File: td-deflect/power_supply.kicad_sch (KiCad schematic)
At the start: 60 parts, among them J13 Conn_01x02_Male, J14 Conn_01x02_Male, J15 Conn_01x02_Male, J18 Conn_01x02_Male, J2 Conn_01x02_Male, J8 Conn_01x02_Male, J9 Conn_01x02_Male, Q12 C2M0045170D, Q13 BSZ42DN25NS3GATMA1, U13 MCP1416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

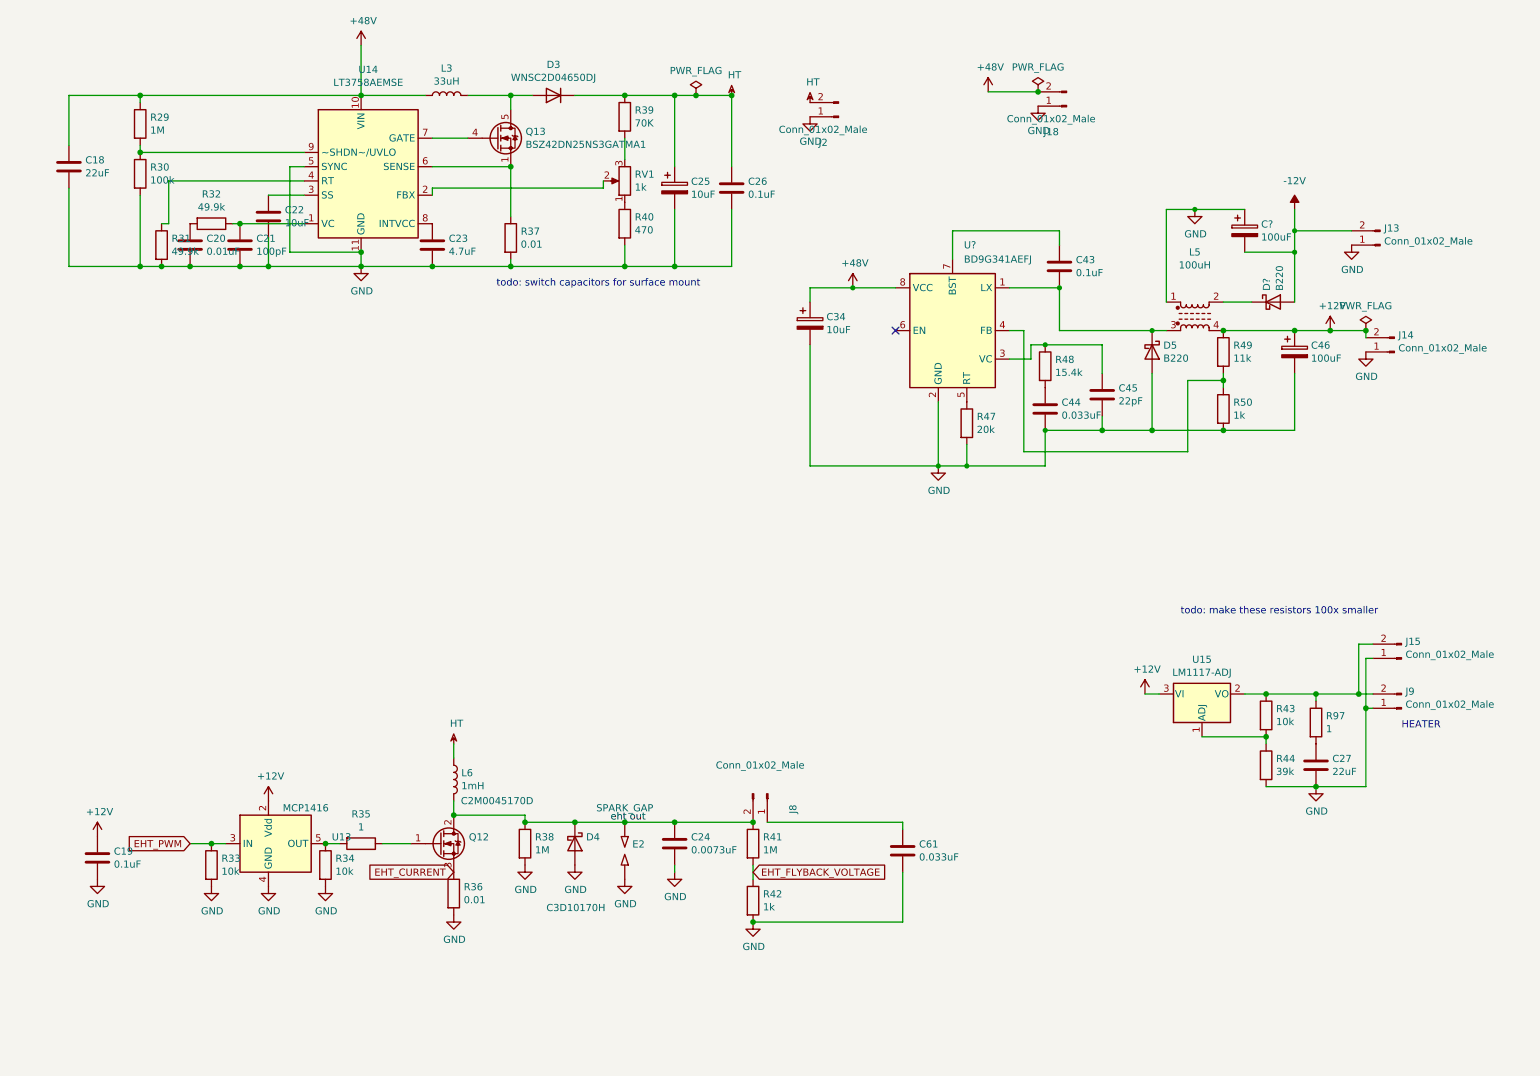
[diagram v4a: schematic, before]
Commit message: add switching heater supply
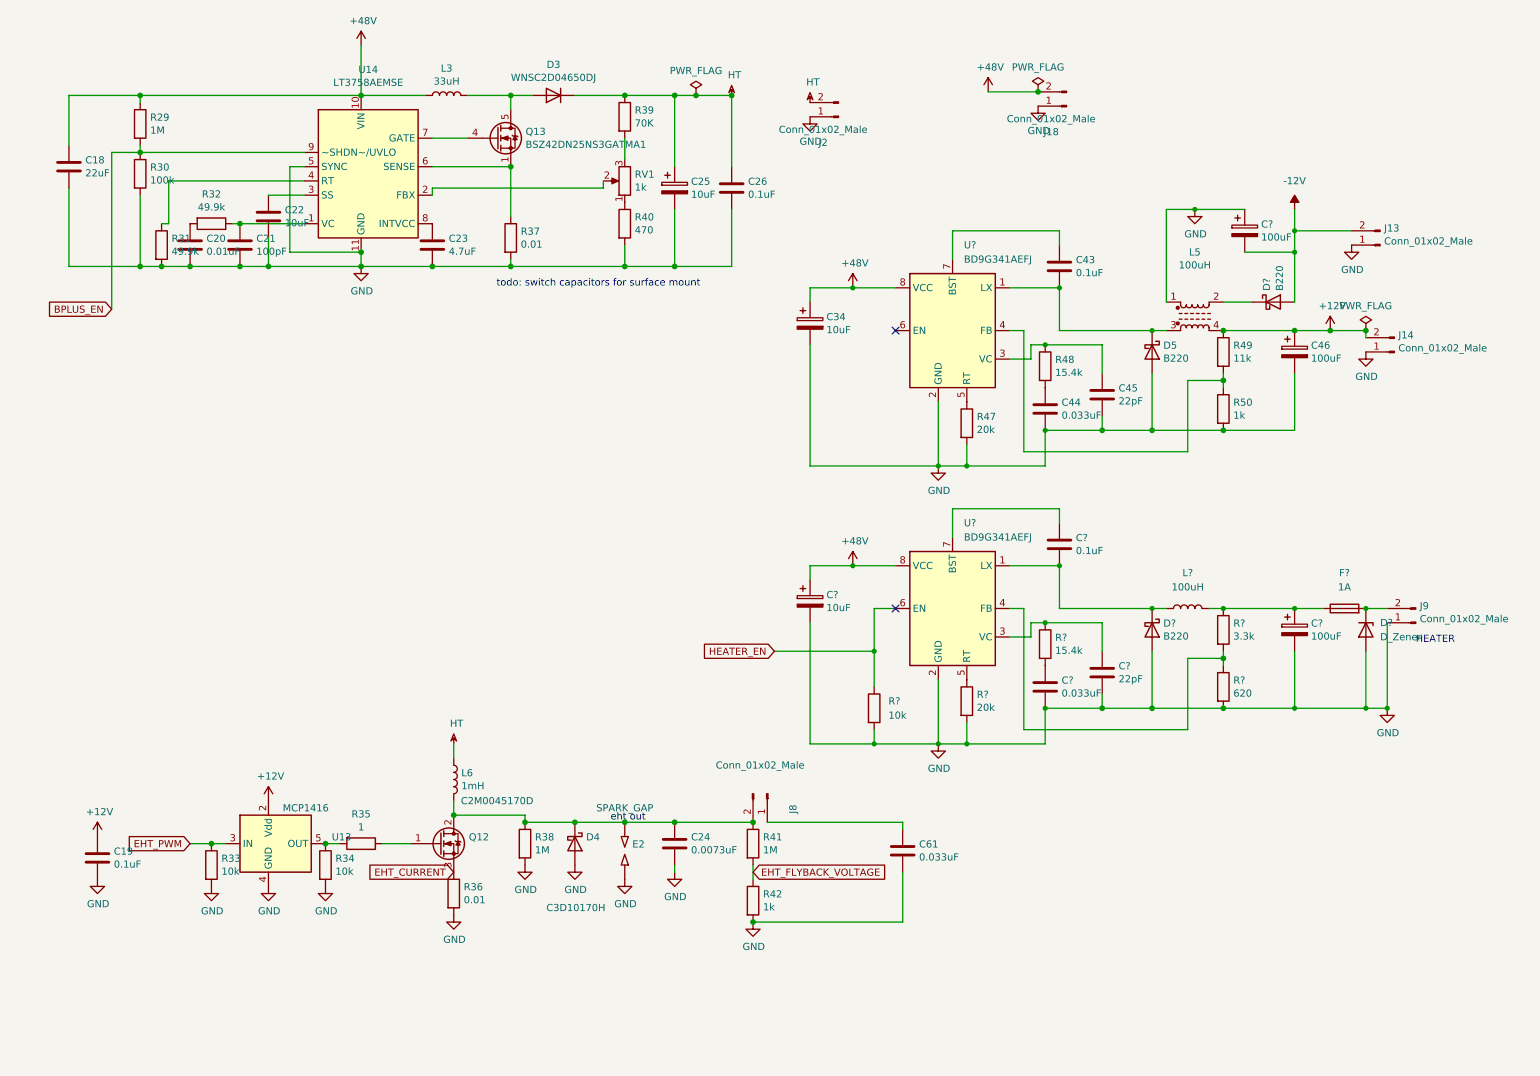
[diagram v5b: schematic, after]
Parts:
- removed C27: 22uF, Capacitor_SMD:C_1206_3216Metric_Pad1.42x1.75mm_HandSolder, symbol Device:C
- removed J15: Conn_01x02_Male, td-deflect:sony_monitor_2p, symbol Connector:Conn_01x02_Male
- removed R43: 10k, Resistor_SMD:R_0805_2012Metric_Pad1.15x1.40mm_HandSolder, symbol Device:R
- removed R44: 39k, Resistor_SMD:R_0805_2012Metric_Pad1.15x1.40mm_HandSolder, symbol Device:R
- removed R97: 1, Resistor_SMD:R_0805_2012Metric_Pad1.15x1.40mm_HandSolder, symbol Device:R
- removed U15: LM1117-ADJ, Package_TO_SOT_SMD:TO-252-2, symbol Regulator_Linear:LM1117-ADJ
- added C?: 0.1uF, Capacitor_SMD:C_0805_2012Metric_Pad1.15x1.40mm_HandSolder, symbol Device:C
- added C?: 100uF, Capacitor_THT:CP_Radial_D8.0mm_P3.50mm, symbol Device:CP
- added C?: 0.033uF, Capacitor_SMD:C_0805_2012Metric_Pad1.15x1.40mm_HandSolder, symbol Device:C
- added C?: 22pF, Capacitor_SMD:C_0805_2012Metric_Pad1.15x1.40mm_HandSolder, symbol Device:C
- added C?: 10uF, Capacitor_THT:CP_Radial_D8.0mm_P3.50mm, symbol Device:CP
- added D?: B220, Diode_SMD:D_SMB, symbol Diode:B220
- added D?: D_Zener, symbol Device:D_Zener
- added F?: 1A, symbol Device:Fuse
- added L?: 100uH, symbol Device:L
- added R?: 620, Resistor_SMD:R_0805_2012Metric_Pad1.15x1.40mm_HandSolder, symbol Device:R
- added R?: 15.4k, Resistor_SMD:R_0805_2012Metric_Pad1.15x1.40mm_HandSolder, symbol Device:R
- added R?: 3.3k, Resistor_SMD:R_0805_2012Metric_Pad1.15x1.40mm_HandSolder, symbol Device:R
- added R?: 10k, symbol Device:R
- added R?: 20k, Resistor_SMD:R_0805_2012Metric_Pad1.15x1.40mm_HandSolder, symbol Device:R
- added U?: BD9G341AEFJ, Package_SO:SOIC-8-1EP_3.9x4.9mm_P1.27mm_EP2.41x3.3mm_ThermalVias, symbol Regulator_Switching:BD9G341EFJ
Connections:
- net +48V: now also C?.1, U?.8 (VCC)
- net GND: now also C?.2, C?.2, C?.2, C?.2, D?.2 (A), D?.2 (A), R?.2, R?.2, R?.2, U?.2 (GND)
- net BPLUS_EN: now reaches R29.2, R30.1, U14.9 (~SHDN~/UVLO)
- net at J9.2 (Pin_2): now also D?.1 (K), F?.2
- new net: C?.2, D?.1 (K), L?.1, U?.1 (LX)
- new net: R?.1, R?.2, U?.4 (FB)
- new net: C?.1, U?.7 (BST)
- new net: C?.1, F?.1, L?.2, R?.1
- new net: C?.1, R?.1, U?.3 (VC)
- new net: C?.1, R?.2
- new net: R?.1, U?.5 (RT)
- new net HEATER_EN: R?.1, U?.6 (EN)
- no-connect marks 1 -> 2
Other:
- note removed: "todo: make these resistors 100x smaller"
- moved on the sheet: J9

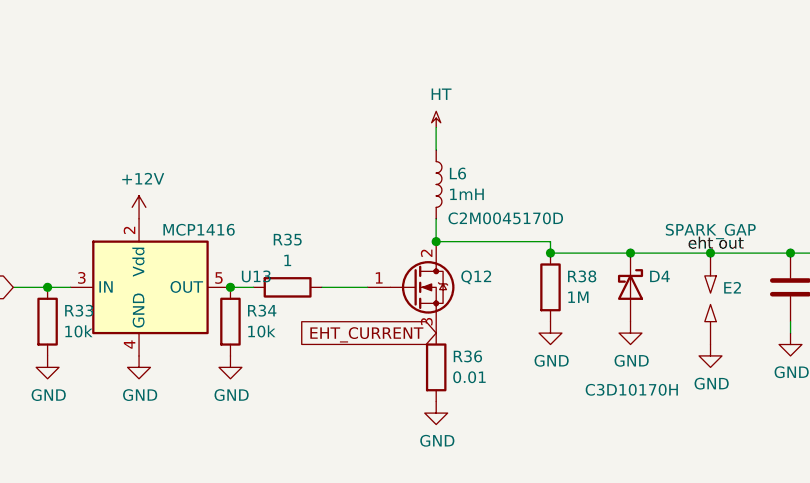
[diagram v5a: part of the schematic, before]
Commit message: switch to new sic for hv
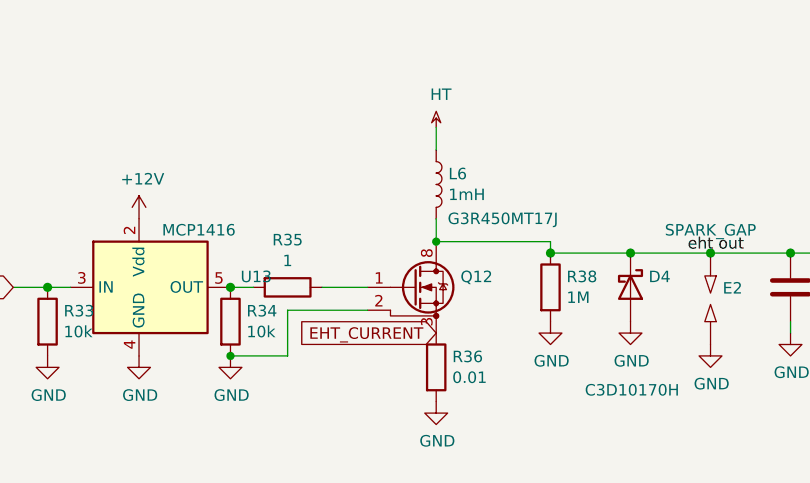
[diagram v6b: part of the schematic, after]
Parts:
- removed Q12: C2M0045170D, Package_TO_SOT_THT:TO-247-3_Vertical, symbol Transistor_FET:C2M0045170D
- added Q12: G3R450MT17J, Package_TO_SOT_SMD:TO-263-7_TabPin8, symbol Transistor_FET:C3M0280090J
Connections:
- net EHT_CURRENT: now also Q12.3 (S), Q12.4 (S), Q12.5 (S), Q12.6 (S), Q12.7 (S)
- net GND: now also Q12.2 (DS)
- net eht out: now also Q12.8 (D)
- net at R35.1: now also Q12.1 (G)
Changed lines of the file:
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@@
   (junction (at 60.96 59.69) (diameter 1.016) (color 0 0 0 0)
   )
+  (junction (at 93.98 157.48) (diameter 0) (color 0 0 0 0)
+  )
   (junction (at 231.14 88.9) (diameter 1.016) (color 0 0 0 0)
   )
@@
   (junction (at 201.93 113.03) (diameter 0) (color 0 0 0 0)
   )
+  (junction (at 71.12 170.18) (diameter 0) (color 0 0 0 0)
+  )
   (junction (at 243.84 53.34) (diameter 0) (color 0 0 0 0)
   )
@@
   )
   (junction (at 201.93 63.5) (diameter 0) (color 0 0 0 0)
-  )
-  (junction (at 93.98 157.48) (diameter 1.016) (color 0 0 0 0)
   )
   (junction (at 55.88 52.07) (diameter 1.016) (color 0 0 0 0)
@@
     (stroke (width 0) (type solid) (color 0 0 0 0))
   )
+  (wire (pts (xy 71.12 170.18) (xy 77.47 170.18))
+    (stroke (width 0) (type default) (color 0 0 0 0))
+  )
   (wire (pts (xy 231.14 66.04) (xy 236.22 66.04))
     (stroke (width 0) (type default) (color 0 0 0 0))
@@
     (stroke (width 0) (type solid) (color 0 0 0 0))
   )
+  (wire (pts (xy 77.47 165.1) (xy 86.36 165.1))
+    (stroke (width 0) (type default) (color 0 0 0 0))
+  )
   (wire (pts (xy 256.54 120.65) (xy 260.35 120.65))
     (stroke (width 0) (type default) (color 0 0 0 0))
@@
   (wire (pts (xy 195.58 120.65) (xy 195.58 142.24))
     (stroke (width 0) (type solid) (color 0 0 0 0))
+  )
+  (wire (pts (xy 77.47 170.18) (xy 77.47 165.1))
+    (stroke (width 0) (type default) (color 0 0 0 0))
   )
   (wire (pts (xy 124.46 55.88) (xy 124.46 59.69))
@@
     (pin "1")
   )
-  (symbol (lib_id "Transistor_FET:C2M0045170D") (at 91.44 162.56 0) (unit 1)
-    (in_bom yes) (on_board yes)
-    (property "Reference" "Q12" (id 0) (at 96.6724 161.3916 0)
-      (effects (font (size 1.27 1.27)) (justify left))
-    )
-    (property "Value" "C2M0045170D" (id 1) (at 95.25 154.94 0)
-      (effects (font (size 1.27 1.27)) (justify left))
-    )
-    (property "Footprint" "Package_TO_SOT_THT:TO-247-3_Vertical" (id 2) (at 91.44 162.56 0)
-      (effects (font (size 1.27 1.27) italic) hide)
-    )
-    (property "Datasheet" "https://www.wolfspeed.com/media/downloads/960/C2M0045170D.000.pdf" (id 3) (at 91.44 162.56 0)
-      (effects (font (size 1.27 1.27)) (justify left) hide)
-    )
-    (property "Digikey" "C2M0045170D-ND" (id 4) (at 91.44 162.56 0)
-      (effects (font (size 1.27 1.27)) hide)
-    )
-    (pin "1")
-    (pin "2")
-    (pin "3")
-  )
   (symbol (lib_id "Device:R") (at 77.47 162.56 270) (unit 1)
     (in_bom yes) (on_board yes)
@@
     (pin "2")
   )
+  (symbol (lib_id "Transistor_FET:C3M0280090J") (at 91.44 162.56 0) (unit 1)
+    (in_bom yes) (on_board yes)
+    (property "Reference" "Q12" (id 0) (at 96.6724 161.3916 0)
+      (effects (font (size 1.27 1.27)) (justify left))
+    )
+    (property "Value" "G3R450MT17J" (id 1) (at 95.25 154.94 0)
+      (effects (font (size 1.27 1.27)) (justify left))
+    )
+    (property "Footprint" "Package_TO_SOT_SMD:TO-263-7_TabPin8" (id 2) (at 91.44 162.56 0)
+      (effects (font (size 1.27 1.27) italic) hide)
+    )
+    (property "Datasheet" "https://genesicsemi.com/sic-mosfet/G3R450MT17J/G3R450MT17J.pdf" (id 3) (at 91.44 162.56 0)
+      (effects (font (size 1.27 1.27)) (justify left) hide)
+    )
+    (property "Digikey" "1242-G3R450MT17J-ND" (id 4) (at 91.44 162.56 0)
+      (effects (font (size 1.27 1.27)) hide)
+    )
+    (pin "1")
+    (pin "2")
+    (pin "3")
+    (pin "4")
+    (pin "5")
+    (pin "6")
+    (pin "7")
+    (pin "8")
+  )
   (symbol (lib_id "Regulator_Switching:BD9G341EFJ") (at 182.88 120.65 0) (unit 1)

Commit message: more hv stuff
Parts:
- removed C61: 0.033uF, Capacitor_SMD:C_1206_3216Metric_Pad1.42x1.75mm_HandSolder, symbol Device:C
- removed D4: C3D10170H, Package_TO_SOT_THT:TO-247-2_Vertical, symbol Diode:C3D10170H
- removed J8: Conn_01x02_Male, Connector_Phoenix_MSTB:PhoenixContact_MSTBVA_2,5_2-G_1x02_P5.00mm_Vertical, symbol Connector:Conn_01x02_Male
- removed L6: 1mH, Inductor_THT:L_Toroid_Vertical_L31.8mm_W15.9mm_P13.50mm_Bourns_5700, symbol Device:L
- added C? (x2): C, symbol Device:C
- added C? (x2): 0.1uF, Capacitor_SMD:C_0805_2012Metric_Pad1.15x1.40mm_HandSolder, symbol Device:C
- added D?: D, symbol Device:D
- added D?: ES1G-13-F, Diode_SMD:D_SMA, symbol Diode:BA157
- added L?: 053X0528-001, symbol td-hv:053X0528-001
- added Q? (x2): BSZ42DN25NS3GATMA1, Package_TO_SOT_SMD:TDSON-8-1, symbol Transistor_FET:BSC082N10LSG
- added R? (x2): 1, Resistor_SMD:R_0805_2012Metric_Pad1.15x1.40mm_HandSolder, symbol Device:R
- added R?: 1k, symbol Device:R
- added R?: 1, symbol Device:R
- added RV?: R_Potentiometer, symbol Device:R_Potentiometer
- added U?: IRS2005S, Package_SO:SOIC-8_3.9x4.9mm_P1.27mm, symbol Driver_FET:IRS2005S
- added U?: LM2903, symbol Comparator:LM2903
- C24: value 0.0073uF -> 1000pf; Digikey 495-3231-ND -> (none)
- L5: value 100uH -> 47uH; footprint (none) -> Inductor_SMD:L_Bourns_SRF1260; symbol Device:L_Ferrite_Coupled -> Device:L_Ferrite_Coupled_1324; Digikey (none) -> SRF1260-470MCT-ND
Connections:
- net +12V: now also C?.1, D?.2 (A), U?.1 (VCC)
- net GND: now also C?.2, C?.2, Q?.1 (S), Q?.2 (S), Q?.3 (S), R?.2, R?.2, U?.4 (COM)
- net HT: now also C?.1, Q?.5 (D)
- net eht out: now also L?.1
- net at C43.2, D5.1 (K), U?.1 (LX): now also L5.2; no longer L5.3
- net at D?.1 (K): now also L5.3; no longer L5.2
- net EHT_CURRENT renamed EHT_FLYBACK_CURRENT
- new net: C?.1, D?.1 (K)
- new net: R?.2, U?.5 (LO)
- new net: C?.2, L?.2, Q?.1 (S), Q?.2 (S), Q?.3 (S), Q?.5 (D), U?.6 (VS)
- new net: R?.2, U?.7 (HO)
- new net: C?.1, D?.1 (K), U?.8 (VB)
- new net: Q?.4 (G), R?.1 (x2)
- new net: L?.7, R?.1
- new net BEAM_CURRENT: L?.8, R?.1
- new net HV_HI: U?.2 (HIN)
- new net HV_LO: U?.3 (LIN)

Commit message: special hv resistor
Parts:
- removed E2: SPARK_GAP, Resistor_THT:R_Axial_DIN0309_L9.0mm_D3.2mm_P12.70mm_Horizontal, symbol Device:SPARK_GAP
- removed R38: 1M, Resistor_THT:R_Axial_DIN0309_L9.0mm_D3.2mm_P15.24mm_Horizontal, symbol Device:R
- added R?: 1k, symbol Device:R
- added U? (x3): 74HC00, symbol 74xx:74HC00
- added U?: LM2903, symbol Comparator:LM2903
- C?: value C -> 0.1uF
- R41: value 1M -> 1M 3000V; footprint Resistor_THT:R_Axial_DIN0309_L9.0mm_D3.2mm_P15.24mm_Horizontal -> Resistor_SMD:R_2512_6332Metric; Digikey BC4422CT-ND -> CHV2512-FX-1004ELFCT-ND
- RV?: value R_Potentiometer -> 10k
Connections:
- net +12V: now also RV?.3, U?.8 (V+)
- net EHT_PWM: now also U?.2; no longer R33.1, U13.3 (IN)
- net GND: now also C?.2, RV?.1, U?.4 (V-), U?.7 (GND)
- net at C?.1, D?.1 (K): now also U?.2 (-)
- net at RV?.2: now also U?.3 (+)
- net at U?.1: now also R?.2, U?.1
- new net: R33.1, U13.3 (IN), U?.3
- new net: U?.1, U?.2, U?.3
- new net +3.3V: R?.1, U?.14 (VCC)
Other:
- moved on the sheet: C19, C?, D?, RV?
